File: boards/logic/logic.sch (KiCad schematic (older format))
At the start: 40 parts, among them IC1 ATTINY85-S, P1 CONN_01X02, P2 CONN_01X06, P3 CONN_01X14, Q1 Q_NPN_EBC, Q2 Q_NPN_EBC, Q3 Q_NPN_EBC, Q4 Q_NPN_EBC, Q5 Q_NPN_EBC, Q6 Q_NPN_EBC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

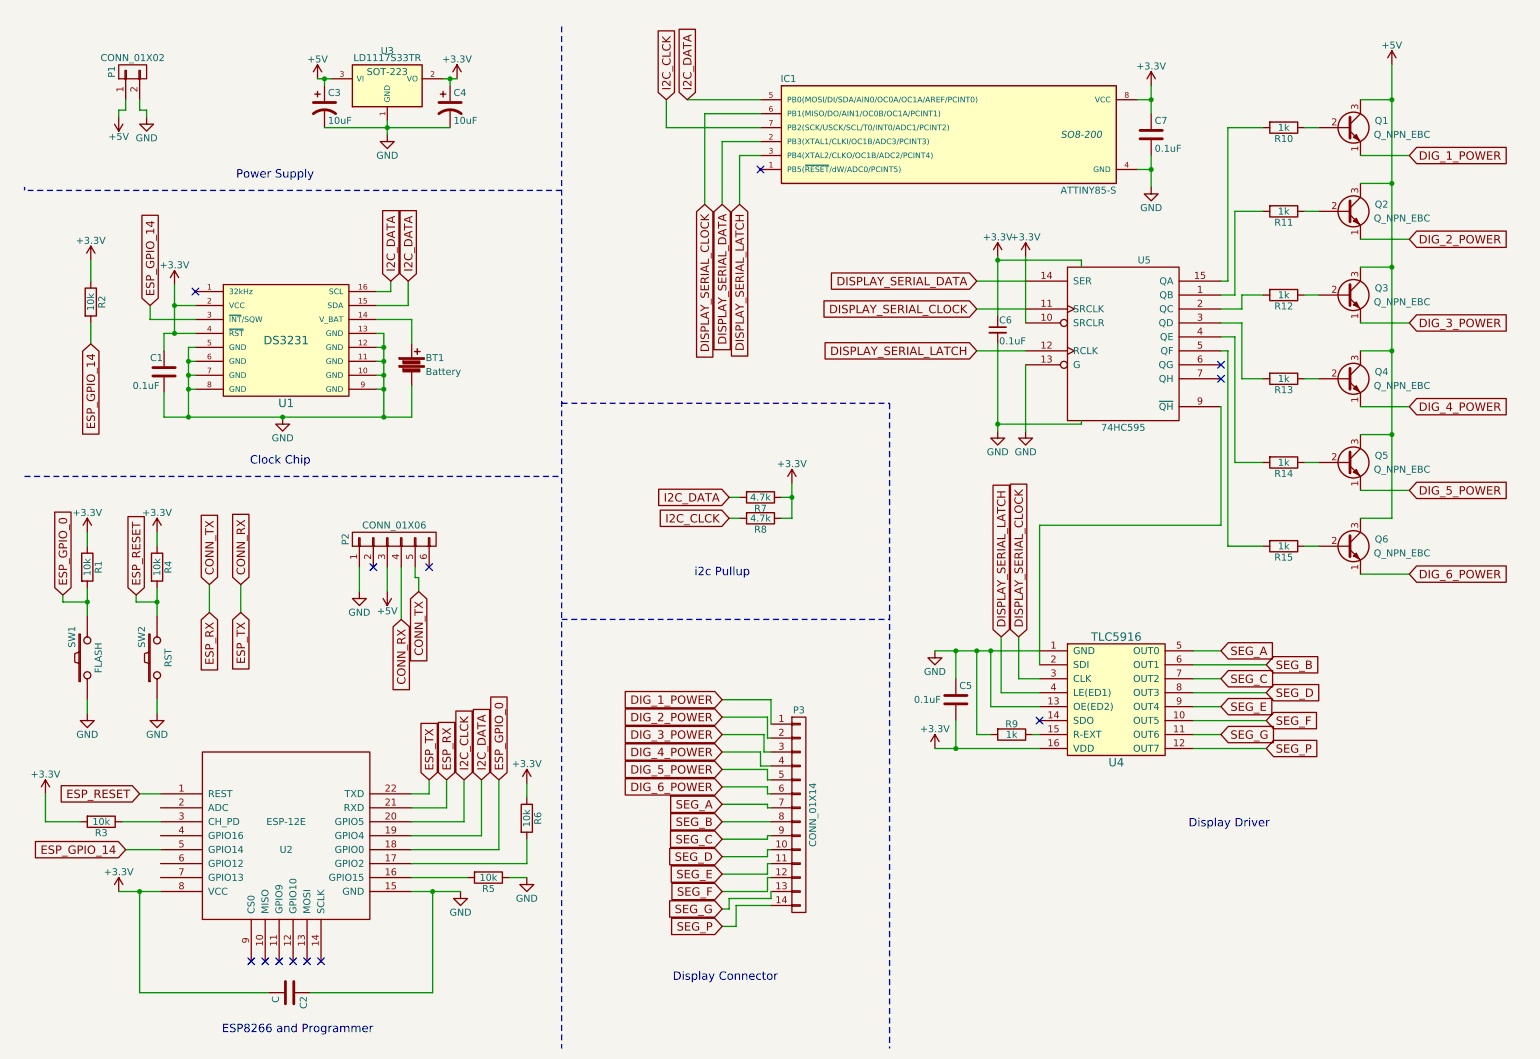
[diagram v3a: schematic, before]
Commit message: Flip the TX/RX on the programming connector.
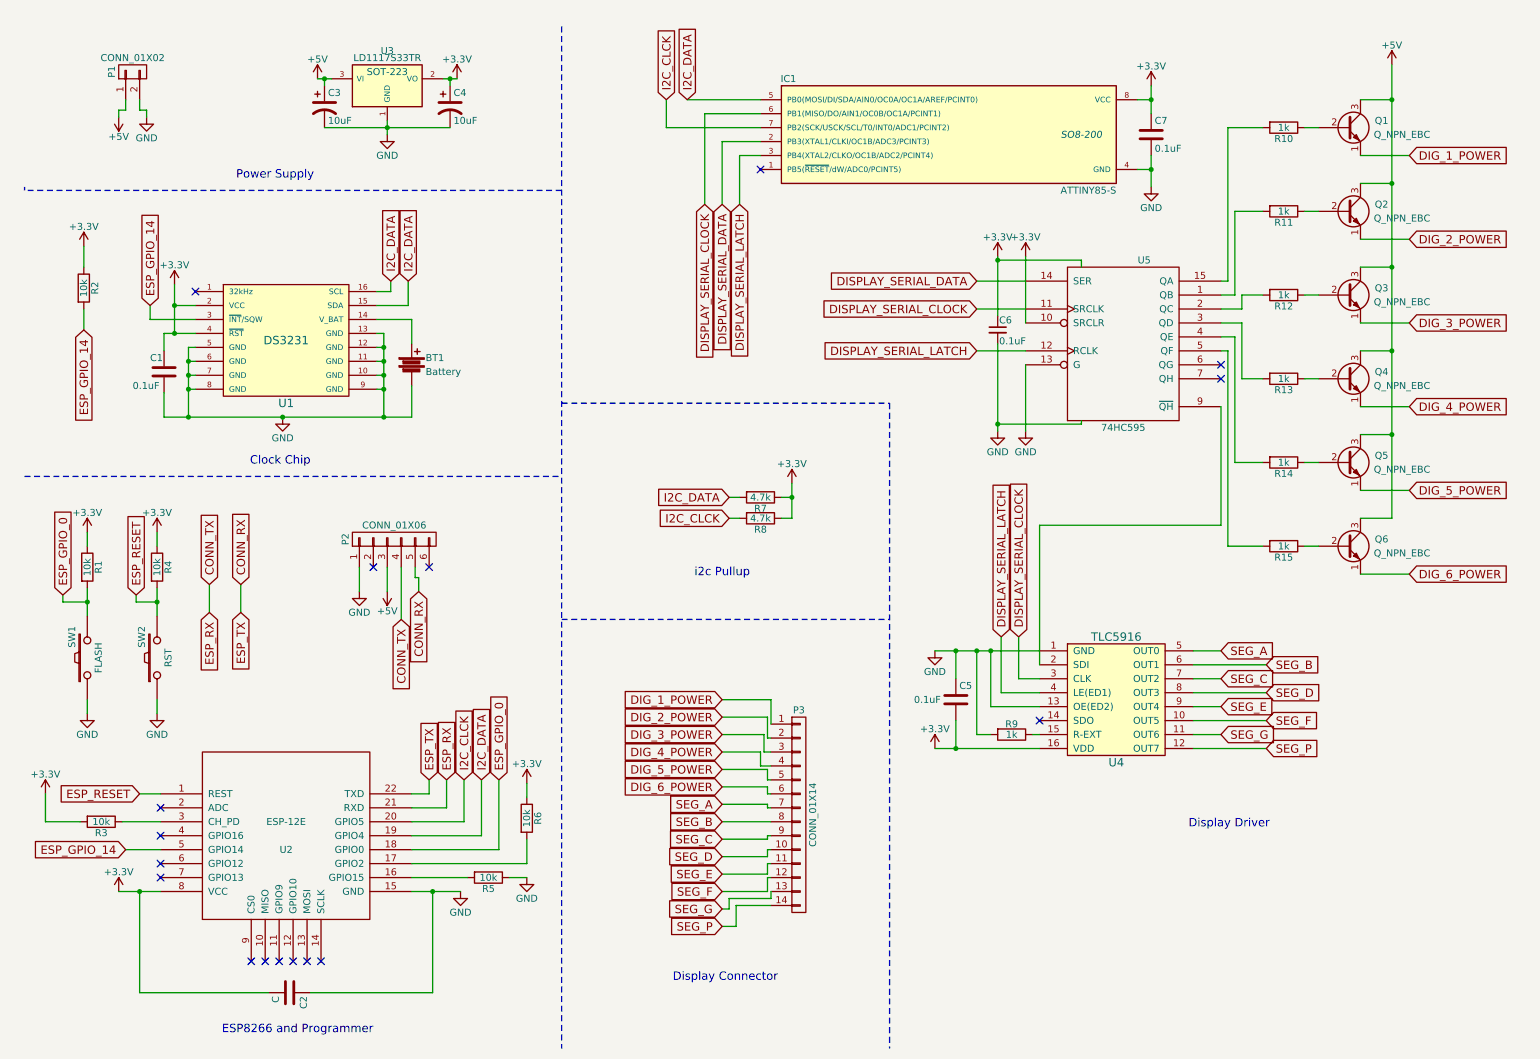
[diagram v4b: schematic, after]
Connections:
- net CONN_RX: now also P2.5 (P5); no longer P2.4 (P4)
- net CONN_TX: now also P2.4 (P4); no longer P2.5 (P5)
- no-connect marks 13 -> 17
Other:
- moved on the sheet: R2
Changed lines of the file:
@@
 	-1   0    0    1
 $EndComp
+Text GLabel 3175 4725 3    60   Input ~ 0
+CONN_TX
 Text GLabel 3300 4525 3    60   Input ~ 0
-CONN_TX
-Text GLabel 3175 4725 3    60   Input ~ 0
 CONN_RX
 NoConn ~ 3375 4350
@@
 	8550 1000 8450 1000
 Wire Wire Line
-	8550 900  8550 1000
-Wire Wire Line
-	8550 1000 8550 1100
-Wire Wire Line
-	8550 1400 8550 1500
-Wire Wire Line
-	8550 1500 8550 1625
+	8550 900  8550 1100
+Wire Wire Line
+	8550 1400 8550 1625
 Wire Wire Line
 	8450 1500 8550 1500
@@
 	7150 5450 7150 5650
 Wire Wire Line
-	7000 5650 7150 5650
-Wire Wire Line
-	7150 5650 7750 5650
-Wire Wire Line
-	7000 4950 7150 4950
-Wire Wire Line
-	7150 4950 7300 4950
-Wire Wire Line
-	7300 4950 7400 4950
-Wire Wire Line
-	7400 4950 7750 4950
+	7000 5650 7750 5650
+Wire Wire Line
+	7000 4950 7750 4950
 Wire Wire Line
 	10050 4400 10400 4400
@@
 	10275 4000 10050 4000
 Wire Wire Line
-	10275 750  10275 1000
-Wire Wire Line
-	10275 1000 10275 1600
-Wire Wire Line
-	10275 1600 10275 2200
-Wire Wire Line
-	10275 2200 10275 2800
-Wire Wire Line
-	10275 2800 10275 3400
-Wire Wire Line
-	10275 3400 10275 4000
+	10275 750  10275 4000
 Wire Wire Line
 	9650 4200 9750 4200
@@
 	9050 2300 9100 2300
 Wire Wire Line
-	7450 2125 7450 2150
-Wire Wire Line
-	7450 2150 7450 2550
+	7450 2125 7450 2550
 Wire Wire Line
 	7450 2150 8050 2150
@@
 Connection ~ 7450 2150
 Wire Wire Line
-	7450 2750 7450 3325
-Wire Wire Line
-	7450 3325 7450 3375
+	7450 2750 7450 3375
 Wire Wire Line
 	7450 3325 8050 3325
@@
 	7300 2800 7650 2800
 Wire Wire Line
-	5975 3750 5975 3850
-Wire Wire Line
-	5975 3850 5975 4000
+	5975 3750 5975 4000
 Wire Wire Line
 	5975 4000 5900 4000
@@
 	925  4200 925  4100
 Wire Wire Line
-	925  4500 925  4600
-Wire Wire Line
-	925  4600 925  4700
+	925  4500 925  4700
 Wire Wire Line
 	750  4600 925  4600
@@
 	1425 4100 1425 4200
 Wire Wire Line
-	1425 4500 1425 4600
-Wire Wire Line
-	1425 4600 1425 4700
+	1425 4500 1425 4700
 Wire Wire Line
 	1275 4550 1275 4600
@@
 	4075 6300 4075 6475
 Wire Wire Line
-	1150 6675 1300 6675
-Wire Wire Line
-	1300 6675 1450 6675
-Wire Wire Line
-	3250 6675 3400 6675
-Wire Wire Line
-	3400 6675 3600 6675
+	1150 6675 1450 6675
+Wire Wire Line
+	3250 6675 3600 6675
 Wire Wire Line
 	1300 6675 1300 7400
@@
 	3225 2475 3225 2300
 Wire Wire Line
-	1550 2325 1550 2475
-Wire Wire Line
-	1550 2475 1550 2675
+	1550 2325 1550 2675
 Wire Wire Line
 	1550 2475 1700 2475
@@
 	1200 6375 1450 6375
 Wire Wire Line
-	1475 2675 1550 2675
-Wire Wire Line
-	1550 2675 1700 2675
+	1475 2675 1700 2675
 Connection ~ 1550 2475
 Wire Wire Line
 	3000 3075 3050 3075
 Wire Wire Line
-	3050 3275 3050 3075
-Wire Wire Line
-	3050 3075 3050 2975
-Wire Wire Line
-	3050 2975 3050 2875
-Wire Wire Line
-	3050 2875 3050 2775
-Wire Wire Line
-	3050 2775 3050 2675
-Wire Wire Line
-	1475 3275 1650 3275
-Wire Wire Line
-	1650 3275 2325 3275
-Wire Wire Line
-	2325 3275 3050 3275
-Wire Wire Line
-	3050 3275 3250 3275
+	3050 3275 3050 2675
+Wire Wire Line
+	1475 3275 3250 3275
 Wire Wire Line
 	3050 2975 3000 2975
@@
 	1650 3075 1700 3075
 Wire Wire Line
-	1650 2775 1650 2875
-Wire Wire Line
-	1650 2875 1650 2975
-Wire Wire Line
-	1650 2975 1650 3075
-Wire Wire Line
-	1650 3075 1650 3275
+	1650 2775 1650 3275
 Connection ~ 2325 3275
 Wire Wire Line
@@
 	4075 6475 3250 6475
 Wire Wire Line
-	2575 850  2625 850
-Wire Wire Line
-	2625 850  2675 850
+	2575 850  2675 850
 Wire Wire Line
 	2625 850  2625 900
 Connection ~ 2625 850
 Wire Wire Line
-	2625 1200 3075 1200
-Wire Wire Line
-	3075 1200 3525 1200
-Wire Wire Line
-	3075 1150 3075 1200
-Wire Wire Line
-	3075 1200 3075 1250
+	2625 1200 3525 1200
+Wire Wire Line
+	3075 1150 3075 1250
 Connection ~ 3075 1200
 Wire Wire Line
 	3525 900  3525 850
 Wire Wire Line
-	3475 850  3525 850
-Wire Wire Line
-	3525 850  3575 850
+	3475 850  3575 850
 Connection ~ 3525 850
 Wire Wire Line
@@
 L R R2
 U 1 1 57D5FD4D
-P 950 2450
-F 0 "R2" V 1030 2450 50  0000 C CNN
-F 1 "10k" V 950 2450 50  0000 C CNN
-F 2 "" V 880 2450 50  0000 C CNN
-F 3 "" H 950 2450 50  0000 C CNN
-	1    950  2450
+P 900 2350
+F 0 "R2" V 980 2350 50  0000 C CNN
+F 1 "10k" V 900 2350 50  0000 C CNN
+F 2 "" V 830 2350 50  0000 C CNN
+F 3 "" H 900 2350 50  0000 C CNN
+	1    900  2350
 	1    0    0    -1
 $EndComp
-Text GLabel 950  2750 3    60   Input ~ 0
+Text GLabel 900  2650 3    60   Input ~ 0
 ESP_GPIO_14
 $Comp
 L +3.3V #PWR029
 U 1 1 57D5FFC1
-P 950 2150
-F 0 "#PWR029" H 950 2000 50  0001 C CNN
-F 1 "+3.3V" H 950 2290 50  0000 C CNN
-F 2 "" H 950 2150 50  0000 C CNN
-F 3 "" H 950 2150 50  0000 C CNN
-	1    950  2150
+P 900 2050
+F 0 "#PWR029" H 900 1900 50  0001 C CNN
+F 1 "+3.3V" H 900 2190 50  0000 C CNN
+F 2 "" H 900 2050 50  0000 C CNN
+F 3 "" H 900 2050 50  0000 C CNN
+	1    900  2050
 	1    0    0    -1
 $EndComp
 Wire Wire Line
-	950  2150 950  2300
-Wire Wire Line
-	950  2600 950  2750
+	900  2050 900  2200
+Wire Wire Line
+	900  2500 900  2650
+NoConn ~ 1450 6575
+NoConn ~ 1450 6475
+NoConn ~ 1450 6275
+NoConn ~ 1450 6075
 $EndSCHEMATC

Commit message: Label the connector names.
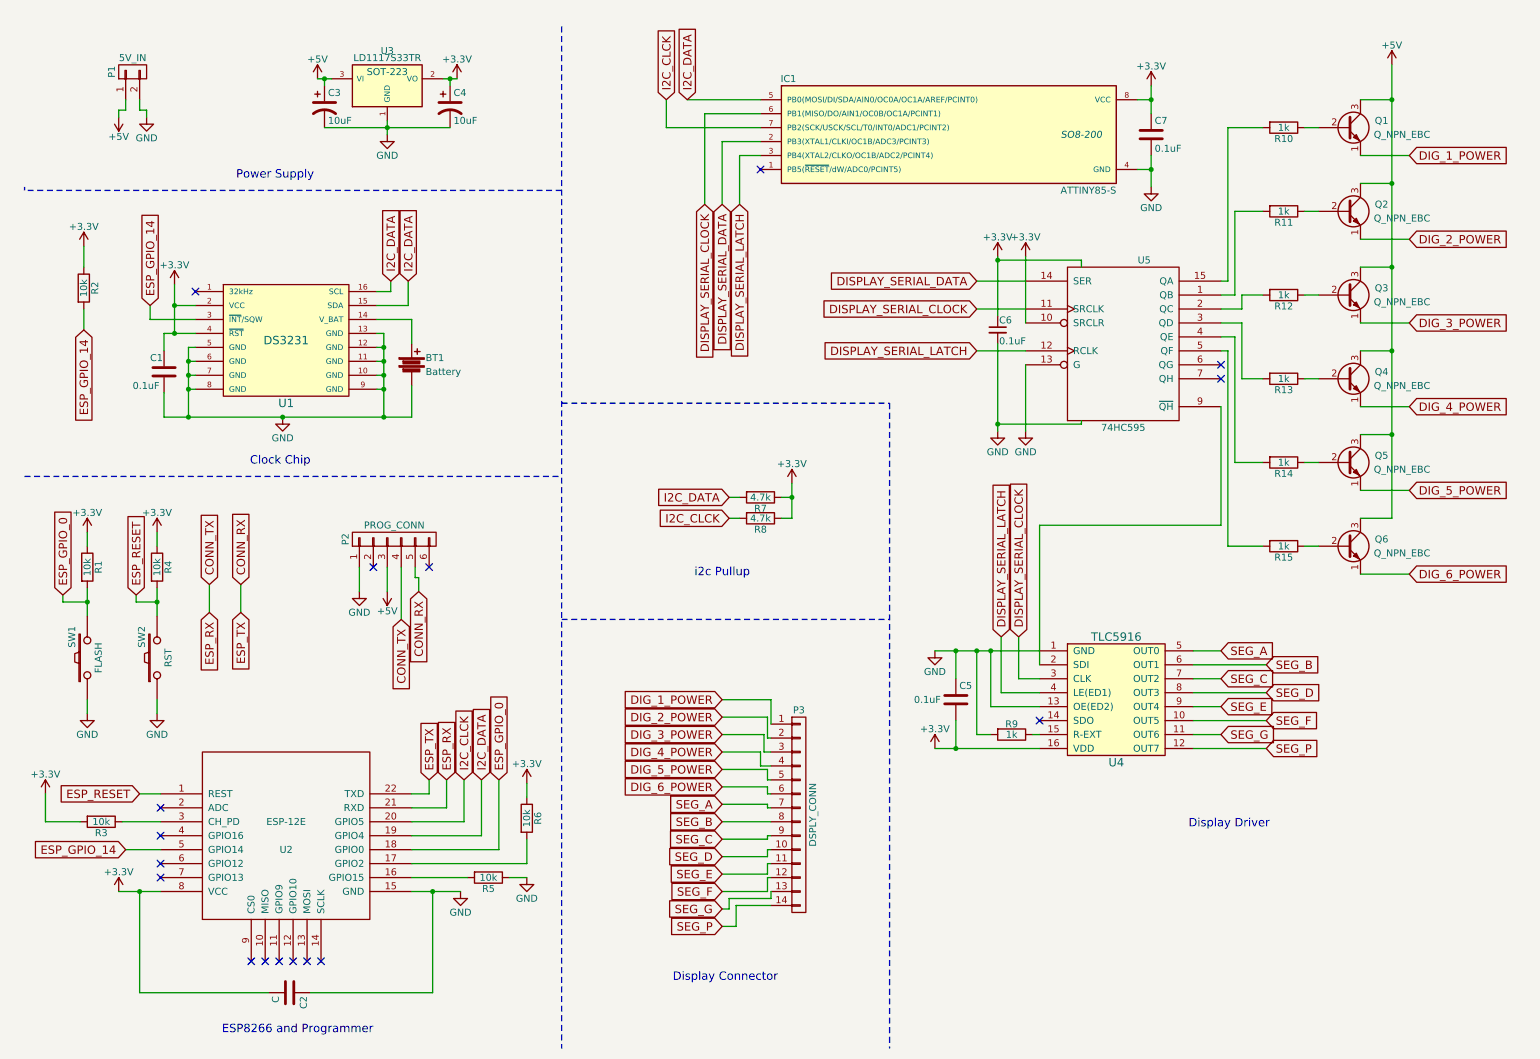
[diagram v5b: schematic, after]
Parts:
- P1: value CONN_01X02 -> 5V_IN
- P2: value CONN_01X06 -> PROG_CONN
- P3: value CONN_01X14 -> DSPLY_CONN
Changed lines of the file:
@@
 P 3125 4150
 F 0 "P2" H 3125 4500 50  0000 C CNN
-F 1 "CONN_01X06" V 3225 4150 50  0000 C CNN
+F 1 "PROG_CONN" V 3225 4150 50  0000 C CNN
 F 2 "" H 3125 4150 50  0000 C CNN
 F 3 "" H 3125 4150 50  0000 C CNN
@@
 P 6025 6125
 F 0 "P3" H 6025 6875 50  0000 C CNN
-F 1 "CONN_01X14" V 6125 6125 50  0000 C CNN
+F 1 "DSPLY_CONN" V 6125 6125 50  0000 C CNN
 F 2 "" H 6025 6125 50  0000 C CNN
 F 3 "" H 6025 6125 50  0000 C CNN
@@
 P 1250 800
 F 0 "P1" H 1250 950 50  0000 C CNN
-F 1 "CONN_01X02" V 1350 800 50  0000 C CNN
+F 1 "5V_IN" V 1350 800 50  0000 C CNN
 F 2 "" H 1250 800 50  0000 C CNN
 F 3 "" H 1250 800 50  0000 C CNN

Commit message: Pull up the display driver reset pin to 3.3V.
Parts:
- added R?: 10k, symbol R
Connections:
- net +3V3: now also R?.1
- net at IC1.1 (PB5(~RESET~/dW/ADC0/PCINT5)): now also R?.2
- no-connect marks 17 -> 16
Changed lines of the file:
@@
 Connection ~ 7400 4950
 NoConn ~ 7750 5450
-NoConn ~ 5750 1500
 $Comp
 L R R2
@@
 NoConn ~ 1450 6275
 NoConn ~ 1450 6075
+$Comp
+L R R?
+U 1 1 57D624FB
+P 6000 2150
+F 0 "R?" V 6080 2150 50  0000 C CNN
+F 1 "10k" V 6000 2150 50  0000 C CNN
+F 2 "" V 5930 2150 50  0000 C CNN
+F 3 "" H 6000 2150 50  0000 C CNN
+	1    6000 2150
+	1    0    0    -1
+$EndComp
+$Comp
+L +3.3V #PWR?
+U 1 1 57D62501
+P 6000 1850
+F 0 "#PWR?" H 6000 1700 50  0001 C CNN
+F 1 "+3.3V" H 6000 1990 50  0000 C CNN
+F 2 "" H 6000 1850 50  0000 C CNN
+F 3 "" H 6000 1850 50  0000 C CNN
+	1    6000 1850
+	1    0    0    -1
+$EndComp
+Wire Wire Line
+	6000 1850 6000 2000
+Wire Wire Line
+	6000 2450 6000 2300
+Wire Wire Line
+	5750 2450 6000 2450
+Wire Wire Line
+	5750 2450 5750 1500
 $EndSCHEMATC

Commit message: Associate footprints with all components.
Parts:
- BT1: footprint (none) -> Connect:CR1220
- C1, C5, C6, C7: footprint (none) -> Capacitors_ThroughHole:C_Disc_D3_P2.5
- C2: value C -> 0.1uF; footprint (none) -> Capacitors_ThroughHole:C_Disc_D3_P2.5
- C3, C4: footprint (none) -> Capacitors_ThroughHole:C_Radial_D5_L6_P2.5
- IC1: footprint SO8-200 -> Housings_DIP:DIP-8_W7.62mm
- P1: footprint (none) -> Pin_Headers:Pin_Header_Straight_1x02
- P2: footprint (none) -> Pin_Headers:Pin_Header_Straight_1x06
- P3: footprint (none) -> Pin_Headers:Pin_Header_Straight_1x14
- Q1, Q2, Q3, Q4, Q5, Q6: footprint (none) -> TO_SOT_Packages_THT:TO-92_Inline_Narrow_Oval
- R1: renamed from R2; footprint (none) -> Resistors_ThroughHole:Resistor_Horizontal_RM10mm
- R10: renamed from R9; footprint (none) -> Resistors_ThroughHole:Resistor_Horizontal_RM10mm
- R11: renamed from R10; footprint (none) -> Resistors_ThroughHole:Resistor_Horizontal_RM10mm
- R12: renamed from R11; footprint (none) -> Resistors_ThroughHole:Resistor_Horizontal_RM10mm
- R13: renamed from R12; footprint (none) -> Resistors_ThroughHole:Resistor_Horizontal_RM10mm
- R14: renamed from R13; footprint (none) -> Resistors_ThroughHole:Resistor_Horizontal_RM10mm
- R15: renamed from R14; footprint (none) -> Resistors_ThroughHole:Resistor_Horizontal_RM10mm
- R16: renamed from R15; footprint (none) -> Resistors_ThroughHole:Resistor_Horizontal_RM10mm
- R2: renamed from R1; footprint (none) -> Resistors_ThroughHole:Resistor_Horizontal_RM10mm
- R3, R4, R5, R6: footprint (none) -> Resistors_ThroughHole:Resistor_Horizontal_RM10mm
- R7, R8: footprint (none) -> Resistors_ThroughHole:Resistor_Horizontal_RM7mm
- R9: renamed from R?; footprint (none) -> Resistors_ThroughHole:Resistor_Horizontal_RM10mm
- SW1, SW2: footprint (none) -> Buttons_Switches_ThroughHole:SW_PUSH_SMALL
- U1: footprint (none) -> Housings_SOIC:SOIC-16_7.5x10.3mm_Pitch1.27mm
- U3: footprint SOT-223 -> TO_SOT_Packages_SMD:SOT-223
- U4, U5: footprint (none) -> Housings_SOIC:SOIC-16_3.9x9.9mm_Pitch1.27mm

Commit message: Update the footprint for the battery holder and densify the PCB layout.
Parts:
- BT1: footprint Connect:CR1220 -> open-project:BAT_CR1216
- U2: footprint (none) -> ESP8266:ESP-12E
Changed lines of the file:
@@
 F 0 "U2" H 2350 6175 50  0000 C CNN
 F 1 "ESP-12E" H 2350 6375 50  0000 C CNN
-F 2 "" H 2350 6275 50  0001 C CNN
+F 2 "ESP8266:ESP-12E" H 2350 6275 50  0001 C CNN
 F 3 "" H 2350 6275 50  0001 C CNN
 	1    2350 6275
@@
 F 0 "BT1" H 3350 2950 50  0000 L CNN
 F 1 "Battery" H 3350 2850 50  0000 L CNN
-F 2 "Connect:CR1220" V 3250 2940 50  0001 C CNN
+F 2 "open-project:BAT_CR1216" V 3250 2940 50  0001 C CNN
 F 3 "" V 3250 2940 50  0000 C CNN
 	1    3250 2900
